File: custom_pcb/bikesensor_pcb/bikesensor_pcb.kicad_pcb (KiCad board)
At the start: 2 copper layers, 72.7 x 167.4 mm, 18 parts, among them J1 ESP32_Left, J2 ESP32_Right, J3 MPU6050, J4 SD_Breakout, J5 NEO-6M_GPS, J6 Conn_01x08_Socket, J7 Conn_01x08_Socket, J8 Conn_01x01, SW1 SW1

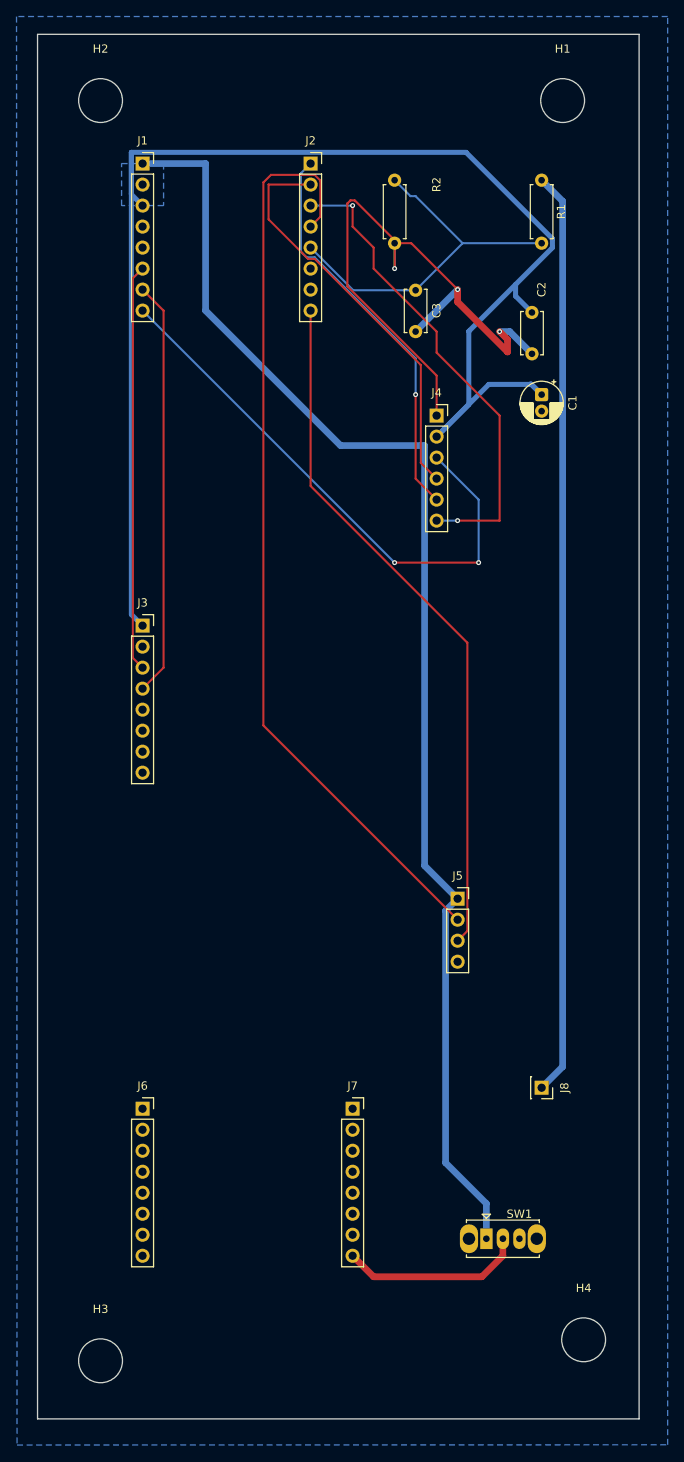
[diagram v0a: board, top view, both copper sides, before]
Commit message: Shrink the carrier board to the real module footprints
Re-lays the board out against the actual ESP32-C3 SuperMini and Wemos
battery shield dimensions: ESP32 rows J1-J2 go 800 -> 600 mil, shield
rows J6-J7 go 1000 -> 900 mil, and the outline drops from 72.75 x 167.43
to 38.74 x 114.47 mm -- the size the README already claimed. Mounting
holes H1-H4 are dropped along with the reclaimed area.

KiCad is not installed on this machine, so this was verified by
rebuilding the connectivity graph straight from the file: every pad sits
at least 1.16 mm inside the board edge, and every net is fully routed
except +3V3, whose track stops 1.48 mm short of C1 pin 1. That bulk cap
is still floating and needs one more track before this is fabbed.

Co-Authored-By: Claude Opus 5 <noreply@anthropic.com>
Claude-Session: https://claude.ai/code/session_01EcNmG8boCU9EBpJGftDikR
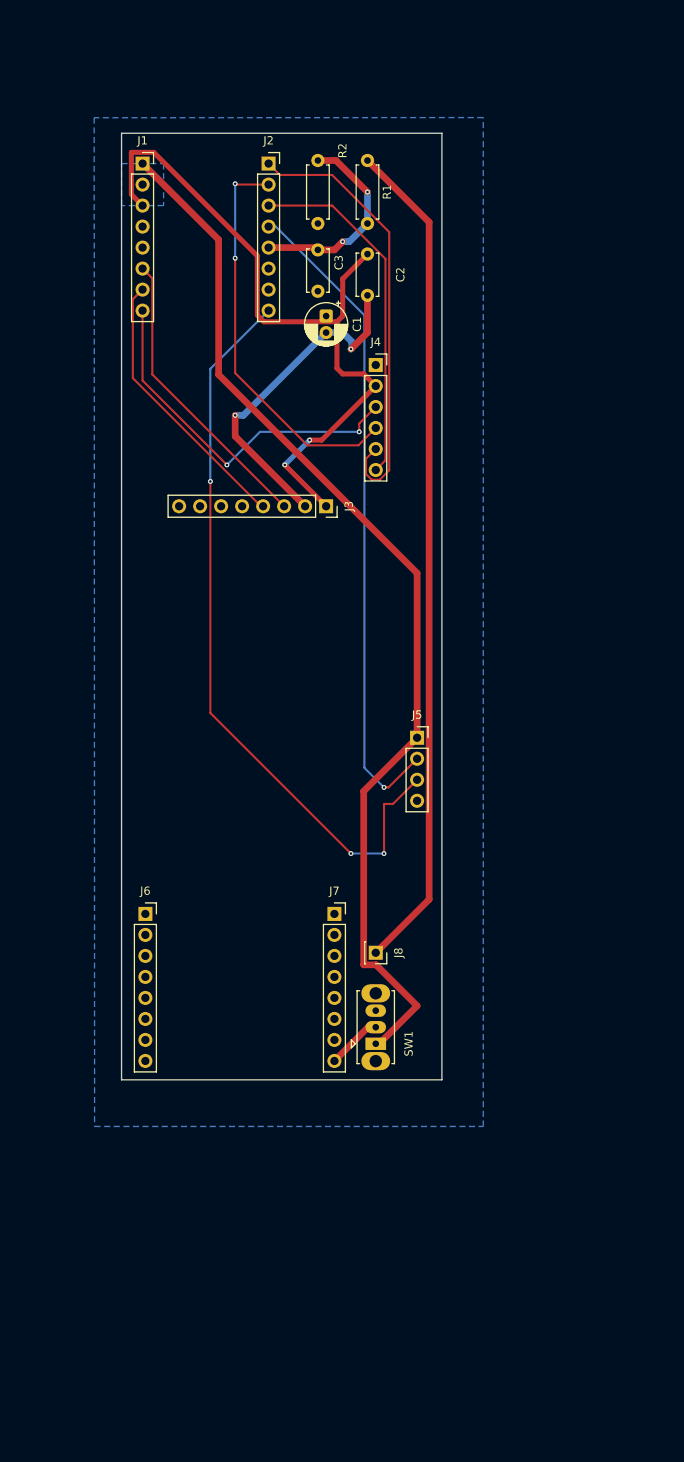
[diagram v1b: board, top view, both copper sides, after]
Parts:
- removed H1, H2, H3, H4: MountingHole, MountingHole:MountingHole_5.3mm_M5
- moved C1 27.7 mm to (73.0, 54.0)
- moved SW1 27.1 mm to (79.0, 142.0), turned to 90 degrees
- moved J3 26.5 mm to (73.0, 77.0), turned to -90 degrees
- moved J8 25.9 mm to (79.0, 131.0)
- moved J7 23.7 mm to (74.0, 126.3)
- moved J6 23.6 mm to (51.1, 126.3)
- moved R1 21.2 mm to (78.0, 35.2)
- moved C2 21.1 mm to (78.0, 46.5)
- moved J5 20.1 mm to (84.0, 105.0)
- moved C3 12.8 mm to (72.0, 46.0)
- moved R2 9.58 mm to (72.0, 35.2)
- moved J4 9.57 mm to (79.0, 59.9)
- moved J2 5.08 mm to (66.0, 35.6)
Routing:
- net +3V3: track 171.6 -> 87.5 mm, vias 0 -> 2
- net GND: track 79.5 -> 41.5 mm, vias 3 -> 2
- net /GPS_TX: track 112.5 -> 79.5 mm, vias 0 -> 1
- net +5V: track 158.9 -> 128.7 mm
- net /SPI_MISO: track 68.1 -> 44.4 mm
- net /BATTERY_ADC: track 43.8 -> 24.8 mm, vias 0 -> 2
- net /I2C_SDA: track 50.4 -> 33.4 mm
- net Net-(J7-Pin_8): track 22.3 -> 6.69 mm
- net /SPI_CS: track 58.2 -> 42.8 mm, vias 2 -> 0
- net /I2C_SCL: track 49.2 -> 35.8 mm
- net /VBAT: track 111.9 -> 101.6 mm
- net /GPS_RX: track 84.5 -> 90.8 mm, vias 0 -> 3
- net /SPI_SCK: track 48.5 -> 53.9 mm, vias 1 -> 0
- net /SPI_MOSI: track 49.5 -> 48.5 mm, vias 0 -> 2
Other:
- board size 72.7 x 167.4 mm -> 38.7 x 114.5 mm

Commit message: Put signal names on the silkscreen
The board had no text on it at all beyond the reference designators, so
assembling or probing it meant counting header pins against a table in
the README. Adds 42 F.SilkS labels generated from the routed netlist: a
short name beside every connected pin on J1-J5, VBAT, the J7 switch
feed, and module names.

Names are abbreviated to fit the 2.54 mm pitch (GTX/GRX for the GPS
UART, DTX/DRX for the debug UART, ADC for the battery divider) at 0.8 mm
height, which is the usual fab minimum. Placement was checked
programmatically: no label overlaps a pad, none collide with each other,
and all sit inside the board outline. Worth an eyeball in KiCad anyway.

Co-Authored-By: Claude Opus 5 <noreply@anthropic.com>
Claude-Session: https://claude.ai/code/session_01EcNmG8boCU9EBpJGftDikR
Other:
- board text added: "3V3"
- board text added: "5V"
- board text added: "AD0"
- board text added: "ADC"
- board text added: "CS"
- board text added: "DRX"
- board text added: "DTX"
- board text added: "ESP32-C3"
- board text added: "GND"
- board text added: "GPS"
- board text added: "GRX"
- board text added: "GTX"
- board text added: "IMU"
- board text added: "INT"
- board text added: "IO8"
- board text added: "IO9"
- board text added: "MISO"
- board text added: "MOSI"
- board text added: "SCK"
- board text added: "SCL"
- board text added: "SD"
- board text added: "SDA"
- board text added: "SHIELD"
- board text added: "VBAT"
- board text added: "XCL"
- board text added: "XDA"

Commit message: Add the CS pull-up and close the two open nets
R3 (10k, /SPI_CS to +3V3) is in the design, and +3V3 now reaches C1
pin 1. Verified from the file rather than from DRC's word for it:
0 unrouted nets across the whole board, and R3's pads land on +3V3
and /SPI_CS.

Also re-aligns the J4 MOSI and SCK silkscreen labels. They had drifted
3.46 mm and 2.92 mm down while the silk overlaps were being cleared,
which put MOSI beside the SCK pin and SCK beside the CS pin -- wiring
the SD card from those labels would have swapped the SPI lines. All six
J4 labels now sit exactly on their pads.

Co-Authored-By: Claude Opus 5 <noreply@anthropic.com>
Claude-Session: https://claude.ai/code/session_01EcNmG8boCU9EBpJGftDikR
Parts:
- added R3: 10k, Resistor_THT:R_Axial_DIN0207_L6.3mm_D2.5mm_P7.62mm_Horizontal, F.Cu at (82.5, 68.9)
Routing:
- net /SPI_CS: track 42.8 -> 54.5 mm, vias 0 -> 1
- net +3V3: track 87.5 -> 95.7 mm, vias 2 -> 3
